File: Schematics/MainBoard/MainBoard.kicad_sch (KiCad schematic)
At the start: 39 parts, among them U1 TC1232, U2 W65C02S6TQG-14, U3 IS62C256AL, U4 IS62C256AL, U5 SST39SF010

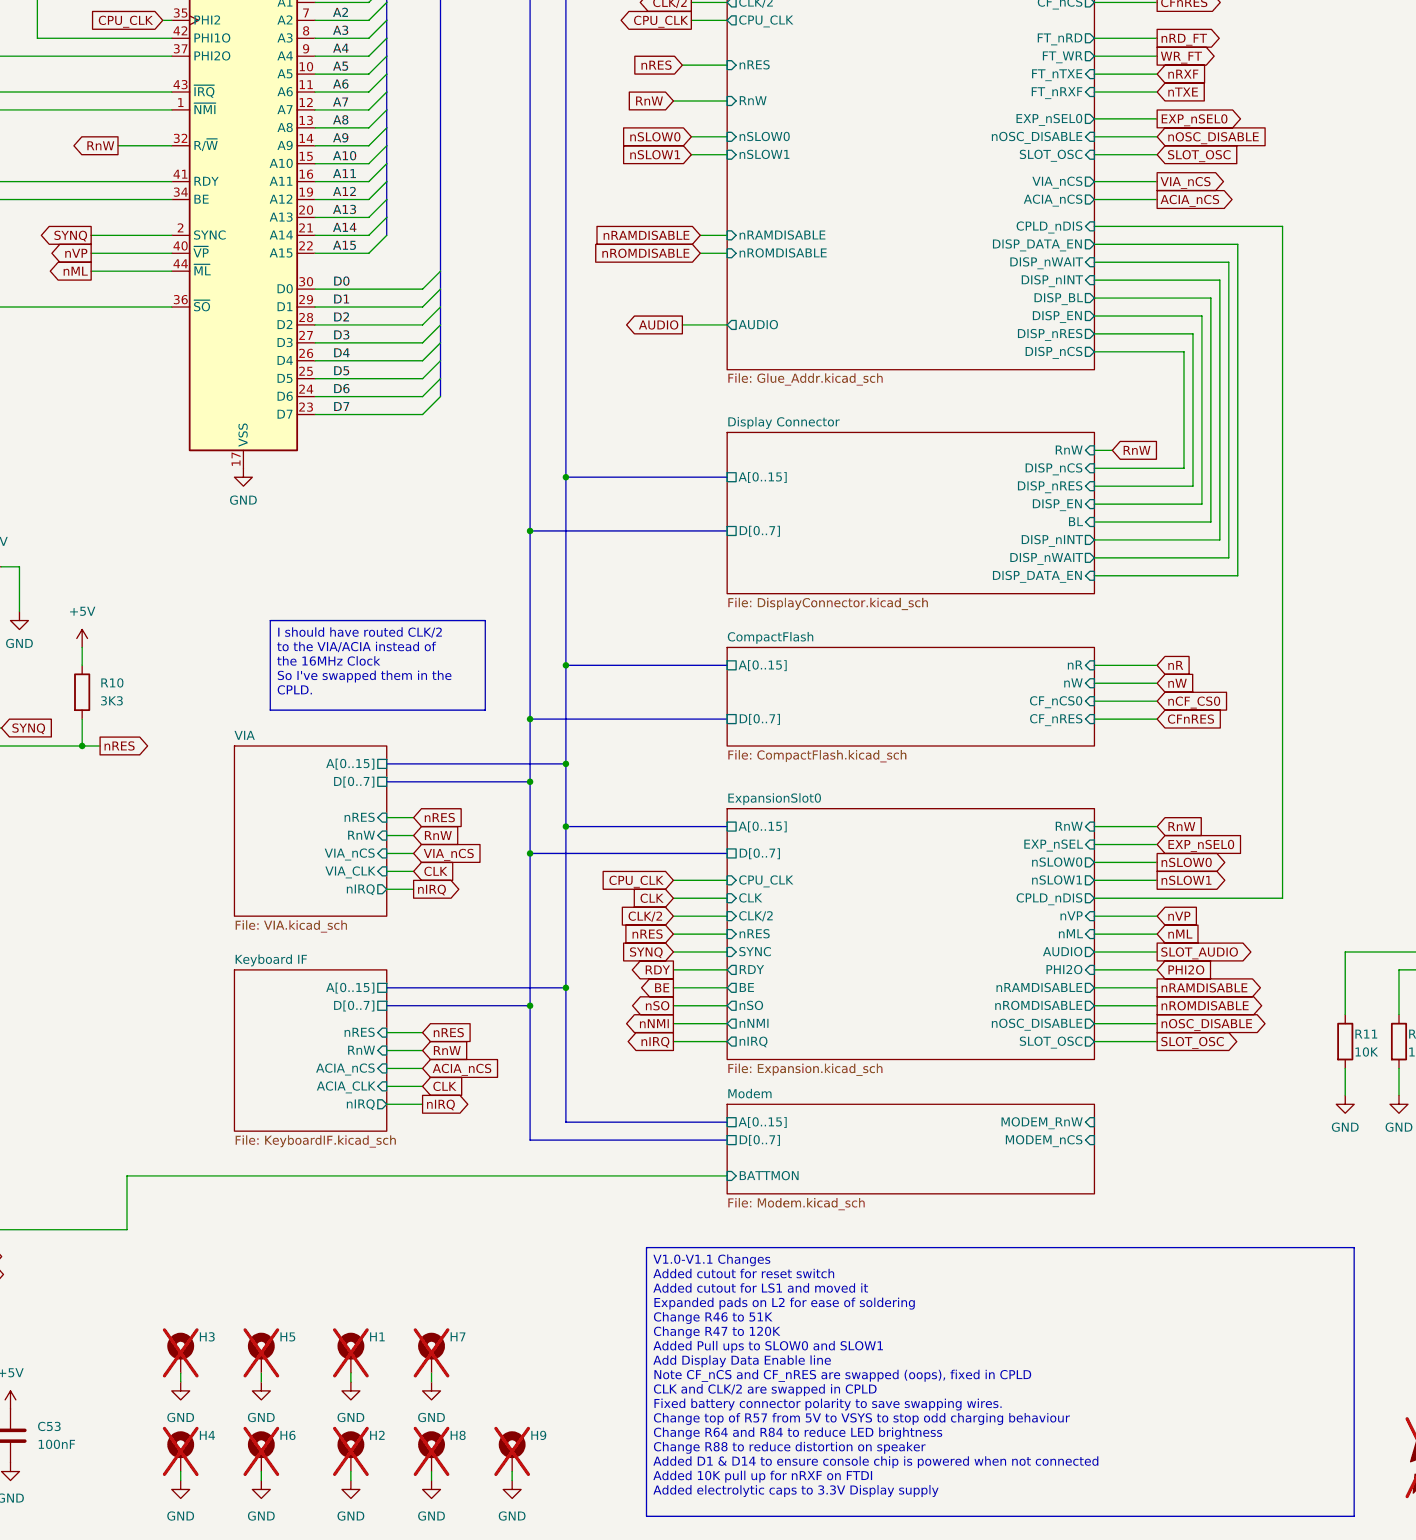
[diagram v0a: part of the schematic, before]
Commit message: Move to a single board for everything (keyboard and main board)
Aim is to save height
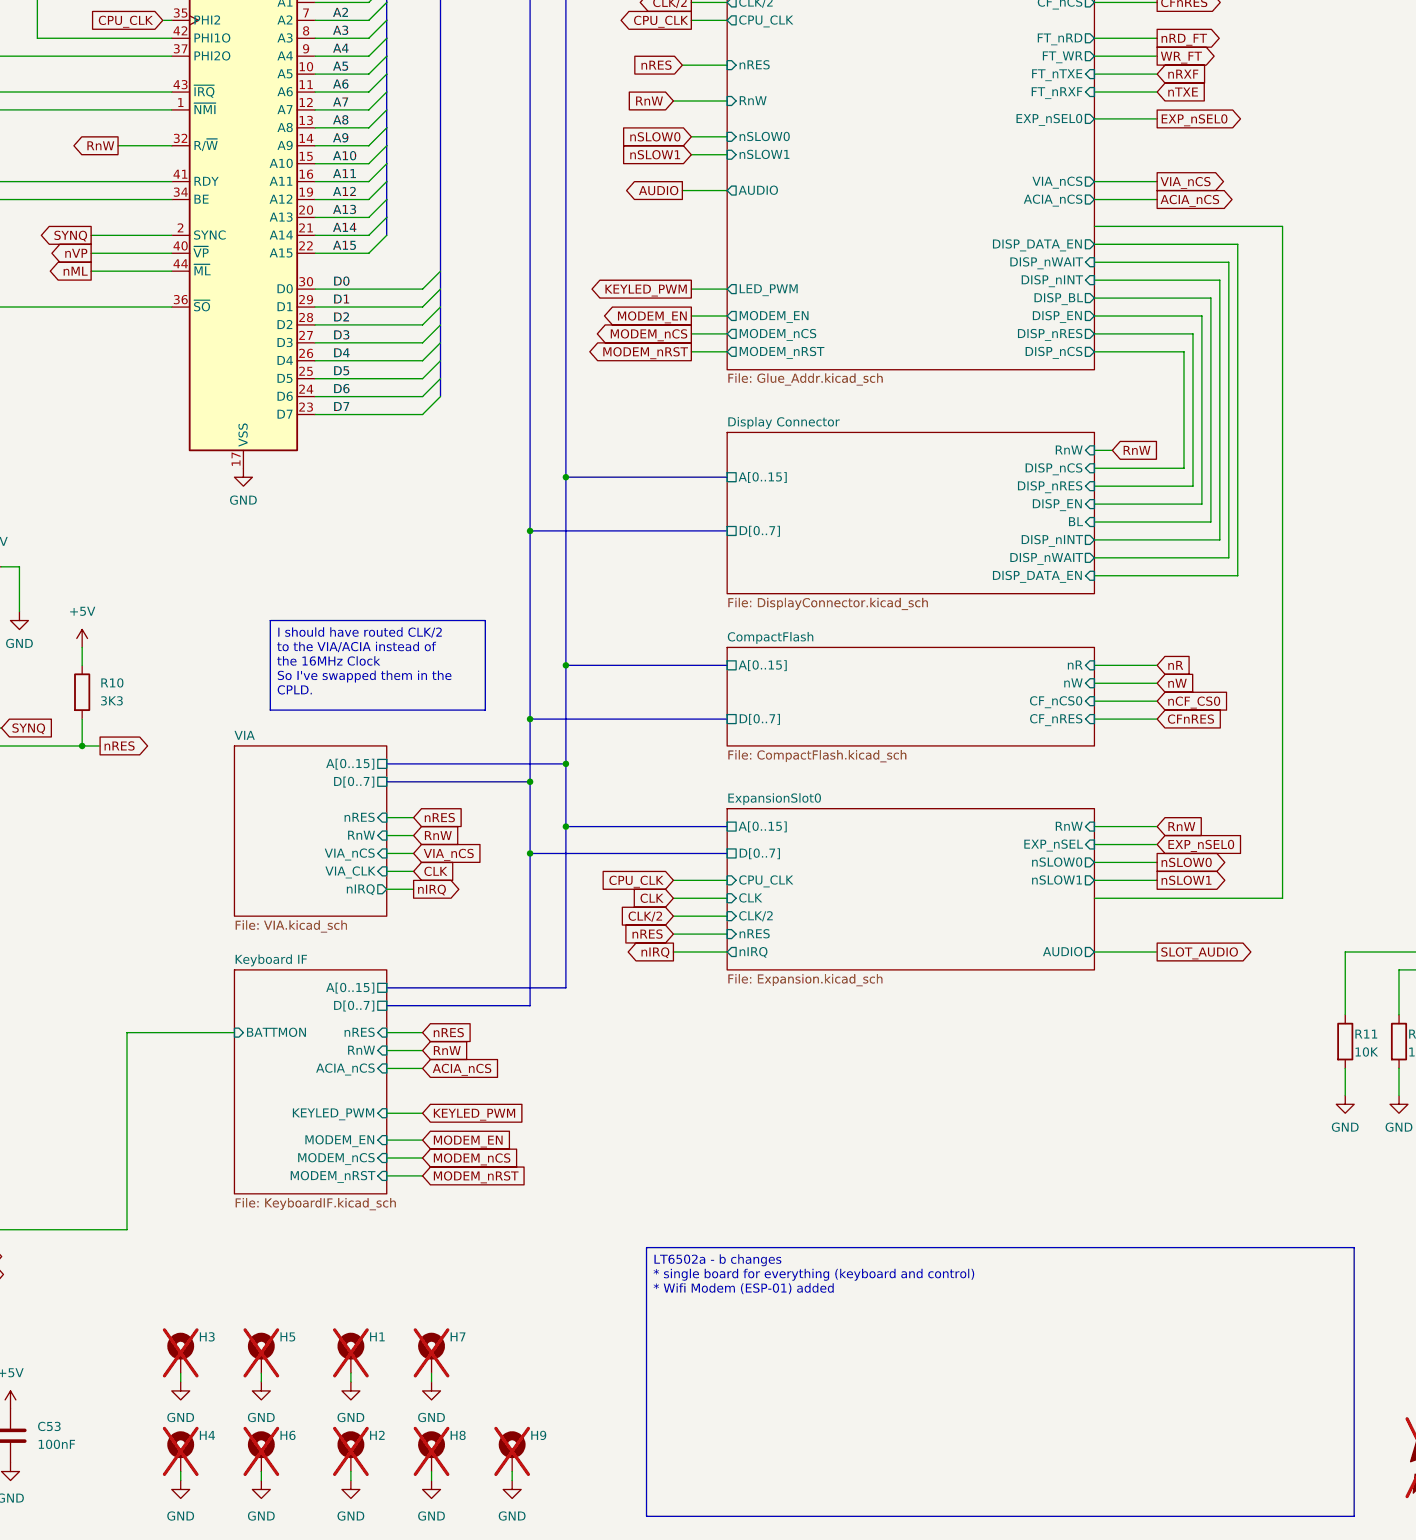
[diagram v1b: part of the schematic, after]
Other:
- removed sheet Modem
- sheet ExpansionSlot0 ports: added none; removed BE, CPLD_nDIS, PHI2O, RDY, SLOT_OSC, SYNC, nML, nNMI, nOSC_DISABLE, nRAMDISABLE, nROMDISABLE, nSO, nVP
- sheet Glue_Addr ports: added LED_PWM, MODEM_EN, MODEM_nCS, MODEM_nRST; removed CPLD_nDIS, SLOT_OSC, nOSC_DISABLE, nRAMDISABLE, nROMDISABLE
- sheet Keyboard IF ports: added BATTMON, KEYLED_PWM, MODEM_EN, MODEM_nCS, MODEM_nRST; removed ACIA_CLK, nIRQ

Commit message: Work on PCB
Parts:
- C1, C2, C3, C4, C5, C53: footprint Capacitor_SMD:C_0603_1608Metric -> Capacitor_SMD:C_0402_1005Metric
- C59: value 250uF 16V -> 100uF 10V Tant; footprint Capacitor_SMD:CP_Elec_10x12.5 -> Capacitor_Tantalum_SMD:CP_EIA-7343-30_AVX-N; LCSC DNF -> DNP; Mouser Part Number 667-EEV-FK1V681Q -> (none)
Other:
- sheet 60FAKE50 ports: added nRES; removed none
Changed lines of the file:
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@@
 	(wire
 		(pts
+			(xy 388.62 182.88) (xy 392.43 182.88)
+		)
+		(stroke
+			(width 0)
+			(type default)
+		)
+	)
+	(wire
+		(pts
 			(xy 50.8 189.23) (xy 53.34 189.23)
 		)
@@
 	(wire
 		(pts
+			(xy 392.43 182.88) (xy 392.43 191.77)
+		)
+		(stroke
+			(width 0)
+			(type default)
+		)
+	)
+	(wire
+		(pts
 			(xy 251.46 53.34) (xy 242.57 53.34)
 		)
@@
 		)
 	)
+	(global_label "nRES"
+		(shape input)
+		(at 388.62 182.88 180)
+		(fields_autoplaced yes)
+		(effects
+			(font
+				(size 1.27 1.27)
+			)
+			(justify right)
+		)
+		(property "Intersheetrefs" "${INTERSHEET_REFS}"
+			(at 380.8573 182.88 0)
+			(effects
+				(font
+					(size 1.27 1.27)
+				)
+				(justify right)
+				(hide yes)
+			)
+		)
+	)
 	(global_label "nSLOW0"
 		(shape input)
@@
 	)
 	(symbol
-		(lib_id "Device:C_Polarized")
-		(at 83.82 142.24 90)
-		(unit 1)
-		(exclude_from_sim no)
-		(in_bom yes)
-		(on_board yes)
-		(dnp no)
-		(property "Reference" "C59"
-			(at 83.82 136.906 90)
-			(effects
-				(font
-					(size 1.27 1.27)
-				)
-			)
-		)
-		(property "Value" "250uF 16V"
-			(at 83.82 138.684 90)
-			(effects
-				(font
-					(size 1.27 1.27)
-				)
-			)
-		)
-		(property "Footprint" "Capacitor_SMD:CP_Elec_10x12.5"
-			(at 87.63 141.2748 0)
-			(effects
-				(font
-					(size 1.27 1.27)
-				)
-				(hide yes)
-			)
-		)
-		(property "Datasheet" "~"
-			(at 83.82 142.24 0)
-			(effects
-				(font
-					(size 1.27 1.27)
-				)
-				(hide yes)
-			)
-		)
-		(property "Description" "Polarized capacitor"
-			(at 83.82 142.24 0)
-			(effects
-				(font
-					(size 1.27 1.27)
-				)
-				(hide yes)
-			)
-		)
-		(property "Mouser Part Number" "667-EEV-FK1V681Q"
-			(at 83.82 142.24 90)
-			(effects
-				(font
-					(size 1.27 1.27)
-				)
-				(hide yes)
-			)
-		)
-		(property "LCSC" "DNF"
-			(at 83.82 142.24 90)
-			(effects
-				(font
-					(size 1.27 1.27)
-				)
-				(hide yes)
-			)
-		)
-		(pin "1"
-		)
-		(pin "2"
-		)
-		(instances
-			(project "LT6502"
-				(path "/a2243a34-697c-4939-97f7-df548e421864"
-					(reference "C59")
-					(unit 1)
-				)
-			)
-		)
-	)
-	(symbol
 		(lib_id "Device:R")
 		(at 77.47 194.31 90)
@@
 	)
 	(symbol
+		(lib_id "Device:C_Polarized")
+		(at 83.82 142.24 90)
+		(unit 1)
+		(exclude_from_sim no)
+		(in_bom yes)
+		(on_board yes)
+		(dnp no)
+		(property "Reference" "C59"
+			(at 82.042 135.89 90)
+			(effects
+				(font
+					(size 1.27 1.27)
+				)
+			)
+		)
+		(property "Value" "100uF 10V Tant"
+			(at 87.884 137.922 90)
+			(effects
+				(font
+					(size 1.27 1.27)
+				)
+			)
+		)
+		(property "Footprint" "Capacitor_Tantalum_SMD:CP_EIA-7343-30_AVX-N"
+			(at 87.63 141.2748 0)
+			(effects
+				(font
+					(size 1.27 1.27)
+				)
+				(hide yes)
+			)
+		)
+		(property "Datasheet" "~"
+			(at 83.82 142.24 0)
+			(effects
+				(font
+					(size 1.27 1.27)
+				)
+				(hide yes)
+			)
+		)
+		(property "Description" "Polarized capacitor"
+			(at 83.82 142.24 0)
+			(effects
+				(font
+					(size 1.27 1.27)
+				)
+				(hide yes)
+			)
+		)
+		(property "LCSC" "DNP"
+			(at 83.82 142.24 0)
+			(effects
+				(font
+					(size 1.27 1.27)
+				)
+				(hide yes)
+			)
+		)
+		(pin "1"
+		)
+		(pin "2"
+		)
+		(instances
+			(project "MainBoard"
+				(path "/a2243a34-697c-4939-97f7-df548e421864"
+					(reference "C59")
+					(unit 1)
+				)
+			)
+		)
+	)
+	(symbol
 		(lib_id "Mechanical:MountingHole_Pad")
 		(at 160.02 267.97 0)
@@
 			)
 		)
-		(property "Footprint" "Capacitor_SMD:C_0603_1608Metric"
+		(property "Footprint" "Capacitor_SMD:C_0402_1005Metric"
 			(at 53.6448 269.24 0)
 			(effects
@@
 			)
 		)
-		(property "Footprint" "Capacitor_SMD:C_0603_1608Metric"
+		(property "Footprint" "Capacitor_SMD:C_0402_1005Metric"
 			(at 32.7152 269.24 0)
 			(effects
@@
 			)
 		)
-		(property "Footprint" "Capacitor_SMD:C_0603_1608Metric"
+		(property "Footprint" "Capacitor_SMD:C_0402_1005Metric"
 			(at 89.8652 269.24 0)
 			(effects
@@
 			)
 		)
-		(property "Footprint" "Capacitor_SMD:C_0603_1608Metric"
+		(property "Footprint" "Capacitor_SMD:C_0402_1005Metric"
 			(at 24.4348 269.24 0)
 			(effects
@@
 			)
 		)
-		(property "Footprint" "Capacitor_SMD:C_0603_1608Metric"
+		(property "Footprint" "Capacitor_SMD:C_0402_1005Metric"
 			(at 61.9252 269.24 0)
 			(effects
@@
 			)
 		)
-		(property "Footprint" "Capacitor_SMD:C_0603_1608Metric"
+		(property "Footprint" "Capacitor_SMD:C_0402_1005Metric"
 			(at 81.5848 269.24 0)
 			(effects
@@
 			)
 		)
+		(pin "nRES" input
+			(at 392.43 191.77 90)
+			(effects
+				(font
+					(size 1.27 1.27)
+				)
+				(justify right)
+			)
+		)

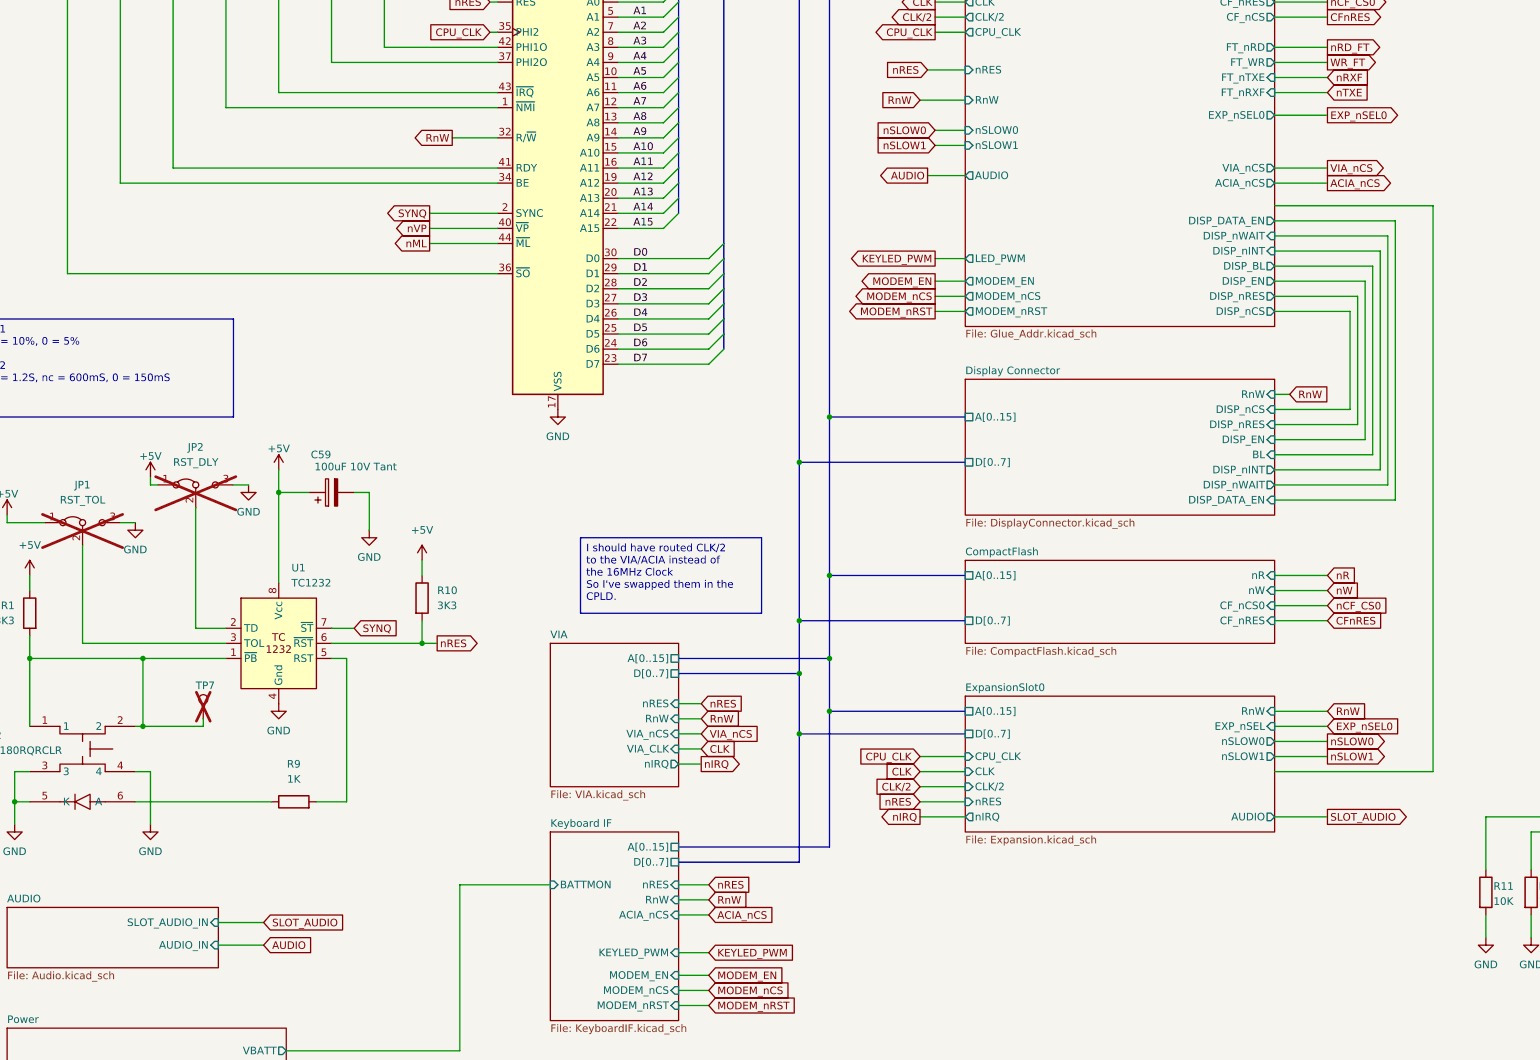
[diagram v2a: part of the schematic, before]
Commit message: Work on PCB routing, added SwinSID
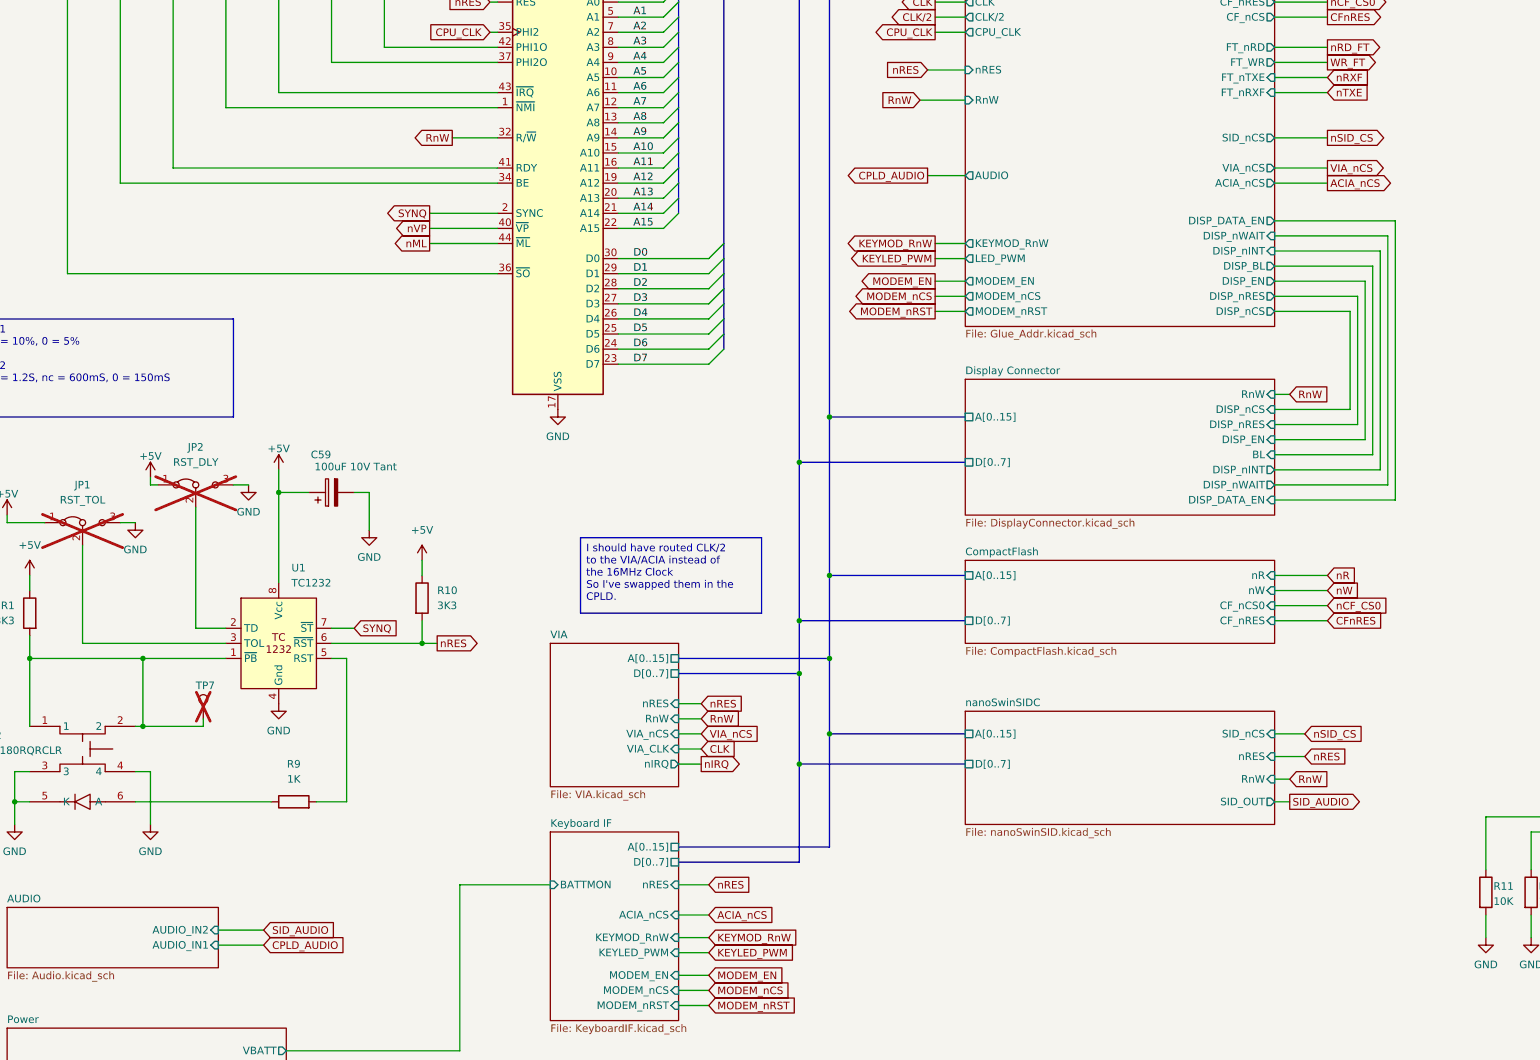
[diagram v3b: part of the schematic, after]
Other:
- removed sheet ExpansionSlot0
- added sheet nanoSwinSIDC (nanoSwinSID.kicad_sch)
- sheet AUDIO ports: added AUDIO_IN1, AUDIO_IN2; removed AUDIO_IN, SLOT_AUDIO_IN
- sheet Glue_Addr ports: added KEYMOD_RnW, SID_nCS; removed EXP_nSEL0, nSLOW0, nSLOW1
- sheet Keyboard IF ports: added KEYMOD_RnW; removed RnW
